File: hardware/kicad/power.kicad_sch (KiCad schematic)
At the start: 46 parts, among them J1 USB_C_Receptacle_USB2.0_16P, J2 BATT (LiFePO4), Q1 AO3401A, U1 MCP73123-22S/MF, U2 TPS63802DLA, U3 TPS61023DRL, U4 TPS22965DSG, U5 USBLC6-2SC6, U6 TPS63900DSK

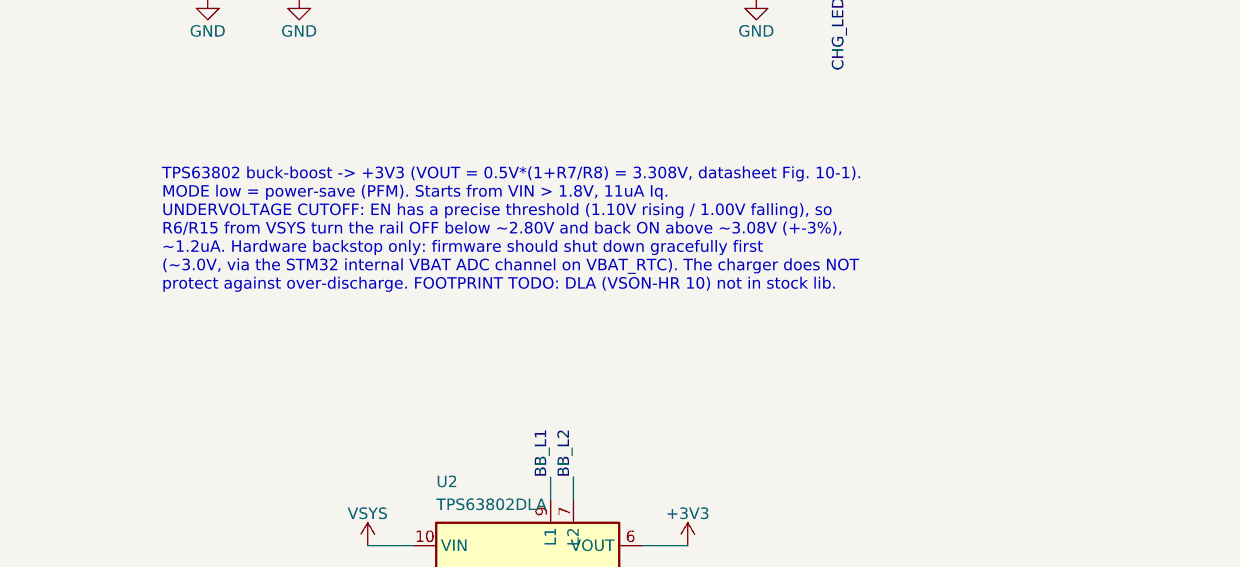
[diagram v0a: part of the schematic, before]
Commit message: Add TPS63802 DLA0010A footprint (project library)
hardware/kicad/epaper.pretty: VSON-HR 10 (2x3 mm HotRod) land pattern
transcribed from the TPS63802 datasheet (SLVSEU9D pp. 35-37), including the
split paste apertures on the pin-8 GND bar (83% coverage). Generated by
hardware/scripts/gen_footprints.py; assigned to U2 via a project
fp-lib-table. ERC 0 violations, power netlist check 34/34.

Co-Authored-By: Claude Opus 5.5 <noreply@anthropic.com>
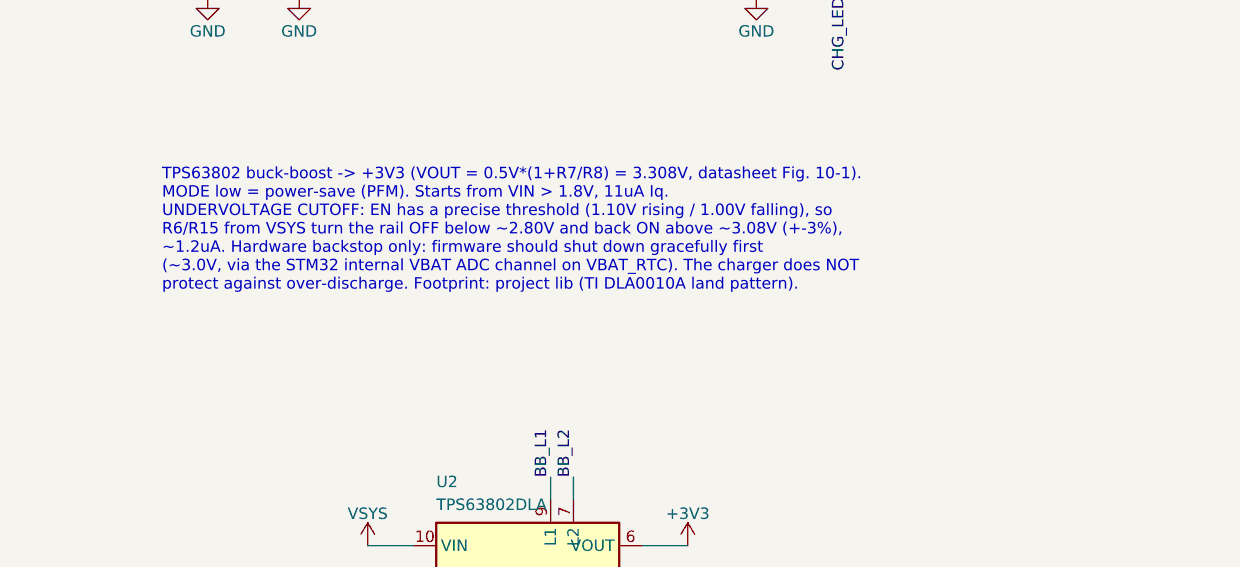
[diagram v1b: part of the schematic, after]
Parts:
- U2: footprint (none) -> epaper:Texas_DLA0010A_VSON-HR-10_2x3mm_P0.5mm
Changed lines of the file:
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@@
 		)
 	)
-	(text "TPS63802 buck-boost -> +3V3 (VOUT = 0.5V*(1+R7/R8) = 3.308V, datasheet Fig. 10-1).\nMODE low = power-save (PFM). Starts from VIN > 1.8V, 11uA Iq.\nUNDERVOLTAGE CUTOFF: EN has a precise threshold (1.10V rising / 1.00V falling), so\nR6/R15 from VSYS turn the rail OFF below ~2.80V and back ON above ~3.08V (+-3%),\n~1.2uA. Hardware backstop only: firmware should shut down gracefully first\n(~3.0V, via the STM32 internal VBAT ADC channel on VBAT_RTC). The charger does NOT\nprotect against over-discharge. FOOTPRINT TODO: DLA (VSON-HR 10) not in stock lib."
+	(text "TPS63802 buck-boost -> +3V3 (VOUT = 0.5V*(1+R7/R8) = 3.308V, datasheet Fig. 10-1).\nMODE low = power-save (PFM). Starts from VIN > 1.8V, 11uA Iq.\nUNDERVOLTAGE CUTOFF: EN has a precise threshold (1.10V rising / 1.00V falling), so\nR6/R15 from VSYS turn the rail OFF below ~2.80V and back ON above ~3.08V (+-3%),\n~1.2uA. Hardware backstop only: firmware should shut down gracefully first\n(~3.0V, via the STM32 internal VBAT ADC channel on VBAT_RTC). The charger does NOT\nprotect against over-discharge. Footprint: project lib (TI DLA0010A land pattern)."
 		(exclude_from_sim no)
 		(at 137.16 129.54 0)
@@
 			)
 		)
-		(property "Footprint" ""
+		(property "Footprint" "epaper:Texas_DLA0010A_VSON-HR-10_2x3mm_P0.5mm"
 			(at 177.8 175.26 0)
 			(hide yes)

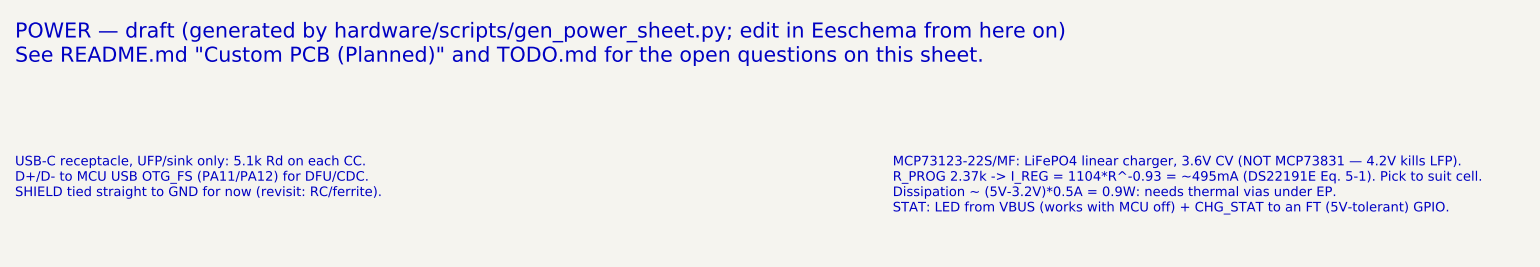
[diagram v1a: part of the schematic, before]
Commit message: Add MCU, Memory and Peripherals sheets; whole-schematic checker
- MCU (A2): STM32F469IIT6 LQFP176. Pin assignment lives in
  sheet_mcu.PINMAP and follows the F469-Disco (FMC SDRAM now 16-bit, QSPI,
  SDIO, SPI1 + HAT control pins, USART3 log UART, I2C1) so the firmware
  config carries over. SD card-detect moved PG2 -> PG10 to keep EXTI2 for
  HRDY. DS11189 power scheme: 13x100nF + 4.7uF, VDDUSB, ferrite-fed
  VDDA/VREF+, 2x2.2uF VCAP; DSI unused per DS11189 2.18 (VDDDSI->VDD,
  VCAPDSI->VDD12DSI, no cap). 8 MHz HSE, 32.768 kHz LSE, BOOT button for
  ROM DFU (BOOT1/PB2 pulled low), TC2050 SWD+SWO, UART header, status LED,
  1k series on the PA9 VBUS sense.
- Memory: IS42S16400J (8 MB), W25Q128JV QSPI, Molex 104031-0811 microSD
  with detect switch and 47k pull-ups, all on 3V3_PERIPH.
- Peripherals: 1x8 header for the external IT8951 HAT (33R series on
  SCK/MOSI/CS), CAP1188 (I2C addr 0x29, 4 electrode pads), PEC11R encoder
  with Bourns' filter, WKUP power button (active high).
- New project symbol CAP1188 and footprint PEC11R-4xxxF-Sxxxx (datasheet
  PCB layout; the Alps EC11E footprint does not fit, its tabs are 11.2 mm
  apart vs 13.2 mm).
- Generator split into common.py + one module per sheet (gen_schematic.py);
  check_schematic.py replaces check_power_netlist.py and adds pin-mux
  (required alternate function per pin), memory-bus end-to-end,
  single-connection-net and pin-vs-footprint-pad checks.

ERC: 0 violations. check_schematic.py: 187 nets, 83 MCU pins, 604 pin/pad
connections OK. All 83 assigned pin numbers also cross-checked by hand
against the DS11189 LQFP176 pin table.

Co-Authored-By: Claude Opus 5.5 <noreply@anthropic.com>
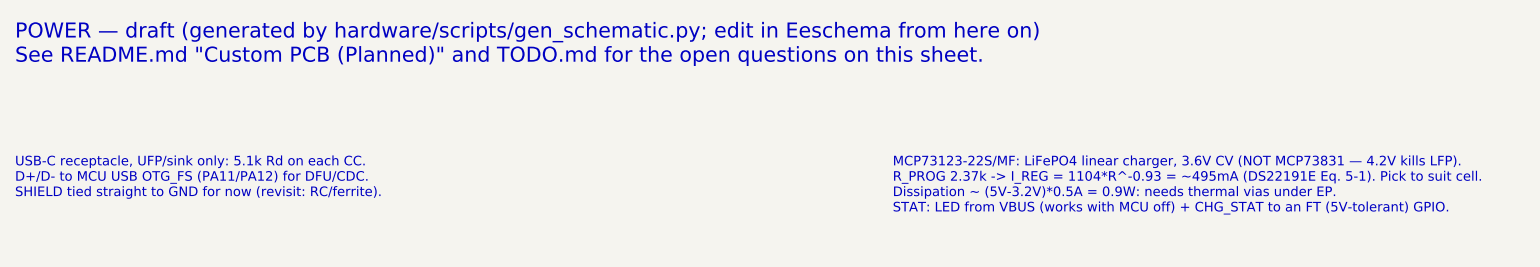
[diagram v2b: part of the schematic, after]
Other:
- note added: "POWER — draft (generated by hardware/scripts/gen_schematic.py; edit in Eeschema from here on) See README.md "Custom PCB (Planned)" and TODO.md for the open questions on this sheet."
- note removed: "POWER — draft (generated by hardware/scripts/gen_power_sheet.py; edit in Eeschema from here on) See README.md "Custom PCB (Planned)" and TODO.md for the open questions on this sheet."

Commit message: Finish v1 schematic: rail test points, docs, deterministic generation
- Power sheet: test points on VBUS/VSYS/+BATT/+3V3/+5V/GND for bring-up;
  R13/R18 0R links (carry all peripheral / MCU current on v1) 0402 -> 0603.
- kicad_gen: UUIDs derived deterministically per sheet (uuid5 of sheet +
  item order), so regenerating produces diffs only where the design changed.
- README: status, pin-assignment table, MCU/memory/peripheral decisions,
  "Checking the Schematic", repo layout. TODO: schematic marked drafted,
  remaining schematic open items (human review, crystals, electrode
  geometry, ESD, HRDY, firmware changes for the custom board), PCB layout
  as the next milestone.

ERC 0 violations; check_schematic.py OK (187 nets, 83 MCU pins, 34
power-sheet nets, all pins present on their footprints).

Co-Authored-By: Claude Opus 5.5 <noreply@anthropic.com>
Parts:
- added TP1: VBUS, TestPoint:TestPoint_Pad_D1.5mm, symbol Connector:TestPoint
- added TP2: VSYS, TestPoint:TestPoint_Pad_D1.5mm, symbol Connector:TestPoint
- added TP3: +BATT, TestPoint:TestPoint_Pad_D1.5mm, symbol Connector:TestPoint
- added TP4: +3V3, TestPoint:TestPoint_Pad_D1.5mm, symbol Connector:TestPoint
- added TP5: +5V, TestPoint:TestPoint_Pad_D1.5mm, symbol Connector:TestPoint
- added TP6: GND, TestPoint:TestPoint_Pad_D1.5mm, symbol Connector:TestPoint
- R13, R18: footprint Resistor_SMD:R_0402_1005Metric -> Resistor_SMD:R_0603_1608Metric
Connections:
- net +3V3: now also TP4.1
- net +5V: now also TP5.1
- net +BATT: now also TP3.1
- net GND: now also TP6.1
- net VBUS: now also TP1.1
- net VSYS: now also TP2.1
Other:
- note added: "Bring-up test points (one per rail)."

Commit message: Switch battery chemistry from LiFePO4 to 1-cell LiPo pouch
Small flat LFP pouches aren't practically buyable in the US; protected LiPo
pouches with JST-PH leads are stocked everywhere.

Power sheet:
- MCP73123 (3.6 V LFP) + discrete AN1149 load sharing (D1/Q1/R5) ->
  TI BQ24073: 4.2 V CV, power path with OUT (VSYS) regulated to 4.4 V so
  the 5.5 V-max TPS63802/TPS61023 stay safe, USB500 input limit, ~500 mA
  charge (ISET 1.78k), ILIM 1.54k fitted (open ILIM disables charging),
  on-board 10k NTC on TS (0-50 C charge window).
- RTC backup: BAT54J -> MCP1700 3.0 V LDO (4.2 V minus a diode drop would
  exceed VBAT's 3.6 V max).
- New VBAT_SENSE 1M/1M divider to PA3 (ADC1_IN3) for the firmware cutoff and
  fuel estimate (VBAT_RTC is now clamped by the LDO).
- UVLO divider on TPS63802 EN 1.8M/1M -> 2.2M/1M (off ~3.20 V, on ~3.52 V).
- MCP73123 project symbol removed; redundant VBAT_RTC PWR_FLAG removed.

README/TODO: chemistry rationale and trade-offs, new power tree, battery
protection layers, updated sheet notes and open items (cell choice, NTC
coupling, fitting the peripheral load switch on v1).

ERC 0 violations; check_schematic.py OK (190 nets, 84 MCU pins, 38 power-
sheet nets); PA3 pin number cross-checked against DS11189.

Co-Authored-By: Claude Opus 5.5 <noreply@anthropic.com>
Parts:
- removed D1: PMEG2010AEH, Diode_SMD:D_SOD-123F, symbol Device:D_Schottky
- removed D3: BAT54J, Diode_SMD:D_SOD-323F, symbol Device:D_Schottky
- removed Q1: AO3401A, Package_TO_SOT_SMD:SOT-23, symbol Transistor_FET:AO3401A
- removed R5: 10k, Resistor_SMD:R_0402_1005Metric, symbol Device:R
- added C15: 10uF, Capacitor_SMD:C_0603_1608Metric, symbol Device:C
- added C16: 1uF, Capacitor_SMD:C_0402_1005Metric, symbol Device:C
- added C17: 100nF, Capacitor_SMD:C_0402_1005Metric, symbol Device:C
- added R19: 1.54k 1%, Resistor_SMD:R_0402_1005Metric, symbol Device:R
- added R20: 100k, Resistor_SMD:R_0402_1005Metric, symbol Device:R
- added R21, R22: 1M 1%, Resistor_SMD:R_0402_1005Metric, symbol Device:R
- added RT1: 10k NTC, Resistor_SMD:R_0402_1005Metric, symbol Device:Thermistor_NTC
- added U7: MCP1700T-3002E/TT, Package_TO_SOT_SMD:SOT-23, symbol Regulator_Linear:MCP1700x-300xxTT
- C1: Voltage (none) -> 10V
- C2: value 4.7uF -> 10uF; Voltage (none) -> 10V
- C3: value 100nF -> 1uF
- J2: value BATT (LiFePO4) -> BATT (1S LiPo)
- R3: value 2.37k 1% -> 1.78k 1%
- R6: value 1.8M 1% -> 2.2M 1%
- U1: value MCP73123-22S/MF -> BQ24073RGT; footprint Package_DFN_QFN:DFN-10-1EP_3x3mm_P0.5mm_EP1.55x2.48mm -> Package_DFN_QFN:VQFN-16-1EP_3x3mm_P0.5mm_EP1.6x1.6mm; symbol epaper:MCP73123 -> Battery_Management:BQ24073RGT; MPN MCP73123-22SI/MF -> BQ24073RGTR
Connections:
- net +BATT: now also U1.2 (BAT), C16.1, R21.1, U7.3 (VI); no longer U1.4 (VBAT)
- net CHG_STAT: now also U1.9 (~{CHG}); no longer U1.7 (STAT)
- net GND: now also U1.15 (TD), U1.17 (VSS), U1.4 (~{CE}), U1.5 (EN2), C15.2, C16.2, C17.2, R19.2, R22.2, RT1.2, U7.1 (GND); no longer U1.11 (EP), U1.9 (VSS)
- net VBAT_RTC: now also U7.2 (VO)
- net VBUS: now also U1.13 (IN), R20.1; no longer U1.1 (VDD), U1.2 (VDD)
- net VSYS: now also U1.10 (OUT), U1.11 (OUT), C15.1
- net CHG_EN1: now reaches U1.6 (EN1)
- net CHG_EN1: now also R20.2
- net PROG renamed ISET
- net ISET: now also U1.16 (ISET); no longer U1.10 (PROG)
- new net ILIM: R19.1, U1.12 (ILIM)
- new net TS: RT1.1, U1.1 (TS)
- new net VBAT_SENSE: C17.1, R21.2, R22.1
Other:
- note added: "BQ24073 1-cell Li-ion/LiPo charger with power path (TI SLUS810N): 4.2V CV, OUT = VSYS regulated to 4.4V with USB present (keeps the 5.5V-max converters safe), battery supplement when the load exceeds the input limit, 6.6V input OVP. ISET 1.78k -> 890/1.78k = ~500mA charge (0.4-0.5C for a 1-1.2Ah cell; retune to cell). EN2=0/EN1=1 -> USB500 input limit (USB-C default power, no CC advertisement rea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"
- note added: "Battery: 1-cell LiPo pouch (3.7V nominal, 4.2V full) WITH a protection board, JST-PH 2.0 lead. J2 pin 1 = + (Adafruit/SparkFun cells: check polarity before plugging in - it is not standardised across vendors). Power path is inside U1, so no discrete load-sharing parts are needed."
- note added: "Cell voltage sense for firmware (fuel estimate + graceful shutdown at ~3.4V): 1M/1M divider -> VBAT_SENSE (4.2V -> 2.1V) to PA3 / ADC1_IN3, 100nF for the ADC sample. ~2uA continuous. (VBAT_RTC can no longer be used: it sits behind the 3.0V LDO.)"
- note added: "RTC backup: cell -> MCP1700 3.0V LDO (1.6uA Iq) -> STM32 VBAT. A full LiPo (4.2V) minus a Schottky drop would still exceed VBAT's 3.6V max. Below ~3.2V the LDO drops out and VBAT tracks the cell (VBAT min 1.65V)."
- note added: "TPS63802 buck-boost -> +3V3 (VOUT = 0.5V*(1+R7/R8) = 3.308V, datasheet Fig. 10-1). MODE low = power-save (PFM). Starts from VIN > 1.8V, 11uA Iq. UNDERVOLTAGE CUTOFF: EN has a precise threshold (1.10V rising / 1.00V falling), so R6/R15 (2.2M/1M) from VSYS turn the rail OFF below ~3.20V and back ON above ~3.52V (+-3%), ~1.1uA. Backstop only: firmware shuts down gracefully first (~3.4V, measured via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"
- note removed: "Battery: JST-PH 2-pin (pin 1 = +). CHECK cell lead polarity — not standardised. Load sharing (Microchip AN1149): with USB present, D1 feeds VSYS from VBUS and Q1 is off, so the charger sees only the cell and terminates correctly. On battery, R5 pulls Q1 gate low -> Q1 on, cell feeds VSYS. R5 = 10k (not 100k) so D1 reverse leakage (tens of uA hot) cannot lift the gate and half-close Q1."
- note removed: "MCP73123-22S/MF: LiFePO4 linear charger, 3.6V CV (NOT MCP73831 — 4.2V kills LFP). R_PROG 2.37k -> I_REG = 1104*R^-0.93 = ~495mA (DS22191E Eq. 5-1). Pick to suit cell. Dissipation ~ (5V-3.2V)*0.5A = 0.9W: needs thermal vias under EP. STAT: LED from VBUS (works with MCU off) + CHG_STAT to an FT (5V-tolerant) GPIO."
- note removed: "RTC backup: cell -> Schottky -> STM32 VBAT. Full LFP 3.65V - ~0.3V drop keeps VBAT under its 3.6V max."
- note removed: "TPS63802 buck-boost -> +3V3 (VOUT = 0.5V*(1+R7/R8) = 3.308V, datasheet Fig. 10-1). MODE low = power-save (PFM). Starts from VIN > 1.8V, 11uA Iq. UNDERVOLTAGE CUTOFF: EN has a precise threshold (1.10V rising / 1.00V falling), so R6/R15 from VSYS turn the rail OFF below ~2.80V and back ON above ~3.08V (+-3%), ~1.2uA. Hardware backstop only: firmware should shut down gracefully first (~3.0V, via the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"

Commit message: Finalize charger for the chosen EEMB cells; battery bay dimensions
From EEMB's LP963450-PCM-LD pack spec and LP603449 cell spec:
- Charge current 500 mA -> ~296 mA (ISET 3.01k, 265-324 mA worst case):
  <= 0.3C of the 1100 mAh cell, EEMB's limit for charging at 0-20 C.
- TMR 72k: fast-charge timer 7.2-12 h (default 4-6 h would expire on the
  1800 mAh cell at ~300 mA).
- Cells allow charging only at 0-45 C; the BQ24073 window is ~0-50 C and TI's
  Rs/Rp network can only widen it (needs an NTC resistance ratio >= 7 across
  the window). So CE -> CHG_DIS (PD6, 100k pull-down keeps charging on with
  the MCU off) and TS -> TS_SENSE (10k/100nF to PC1, ADC1_IN11) for firmware
  supervision of the hot end.
- README: pack specs (PCM 3.0 V over-discharge / 4.28 V overcharge, 1 A
  continuous, 50 mm AWG26 leads), battery bay envelope (52 x 34.5 x 9.9 mm
  max + swelling allowance, lead exit edge), pin table. TODO: firmware
  charge-temperature supervision; arrival checks.

ERC 0 violations; check_schematic.py OK (190 nets, 86 MCU pins, 40 power-
sheet nets); PD6/PC1 pin numbers cross-checked against DS11189.

Co-Authored-By: Claude Opus 5.5 <noreply@anthropic.com>
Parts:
- removed C5, C6: 10uF, Capacitor_SMD:C_0603_1608Metric, symbol Device:C
- removed L1: 0.47uH, Inductor_SMD:L_Murata_DFE201610P, symbol Device:L
- removed L2: 1uH, Inductor_SMD:L_Murata_DFE201610P, symbol Device:L
- removed R14, R17: 100k, Resistor_SMD:R_0402_1005Metric, symbol Device:R
- added C12: 22uF, Capacitor_SMD:C_0805_2012Metric, symbol Device:C
- added C2: 10uF, Capacitor_SMD:C_0603_1608Metric, symbol Device:C
- added C7, C9: 22uF, Capacitor_SMD:C_0603_1608Metric, symbol Device:C
- added R18: 0R, Resistor_SMD:R_0603_1608Metric, symbol Device:R
- added R23: 72k 1%, Resistor_SMD:R_0402_1005Metric, symbol Device:R
- added R24: 100k, Resistor_SMD:R_0402_1005Metric, symbol Device:R
- added R25: 10k, Resistor_SMD:R_0402_1005Metric, symbol Device:R
- added R7: 511k 1%, Resistor_SMD:R_0402_1005Metric, symbol Device:R
- added TP4: +3V3, TestPoint:TestPoint_Pad_D1.5mm, symbol Connector:TestPoint
- C18: renamed from C2; value 10uF -> 100nF; footprint Capacitor_SMD:C_0603_1608Metric -> Capacitor_SMD:C_0402_1005Metric; Voltage 10V -> (none)
- C5: renamed from R7; value 511k 1% -> 10uF; footprint Resistor_SMD:R_0402_1005Metric -> Capacitor_SMD:C_0603_1608Metric; symbol Device:R -> Device:C; Voltage (none) -> 10V
- C6: renamed from C7; value 22uF -> 10uF
- L1: renamed from C9; value 22uF -> 0.47uH; footprint Capacitor_SMD:C_0603_1608Metric -> Inductor_SMD:L_Murata_DFE201610P; symbol Device:C -> Device:L; MPN (none) -> DFE201612E-R47M (TI Table 10-2: 5.5A Isat; verify land patt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
- L2: renamed from C12; value 22uF -> 1uH; footprint Capacitor_SMD:C_0805_2012Metric -> Inductor_SMD:L_Murata_DFE201610P; symbol Device:C -> Device:L; MPN (none) -> DFE201610P-1R0M (verify Isat vs 3.7A valley limit)
- R14: renamed from TP4; value +3V3 -> 100k; footprint TestPoint:TestPoint_Pad_D1.5mm -> Resistor_SMD:R_0402_1005Metric; symbol Connector:TestPoint -> Device:R; now not fitted
- R17: renamed from R18; value 0R -> 100k; footprint Resistor_SMD:R_0603_1608Metric -> Resistor_SMD:R_0402_1005Metric; now not fitted
- R3: value 1.78k 1% -> 3.01k 1%
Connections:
- net +3V3: now also C9.1, R18.1, R7.1, TP4.1; no longer C5.1, L1.1, R14.1, R17.1
- net +5V: now also C12.1; no longer L2.1
- net +BATT: now also C2.1; no longer C18.1
- net 3V3_AON: now also C7.1, R18.2; no longer C6.1, R17.2
- net AON_EN: now also R17.2
- net BB_FB: now also R7.2; no longer C5.2
- net BB_L1: now also L1.1
- net BB_L2: now also L1.2
- net BST_SW: now also L2.2
- net GND: now also C5.2, R14.2, C12.2, C2.2, C7.2, C9.2, R23.2, R24.2; no longer L1.2, L2.2, U1.4 (~{CE})
- net PERIPH_EN: now also R14.1
- net TS: now also R25.1
- net VSYS: now also C5.1, C6.1, L2.1, R17.1
- net TMR: now reaches U1.14 (TMR)
- net TMR: now also R23.1
- new net CHG_DIS: R24.1, U1.4 (~{CE})
- new net TS_SENSE: C18.1, R25.2
- no-connect marks 4 -> 3
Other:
- note added: "BQ24073 1-cell Li-ion/LiPo charger with power path (TI SLUS810N): 4.2V CV, OUT = VSYS regulated to 4.4V with USB present (keeps the 5.5V-max converters safe), battery supplement when the load exceeds the input limit, 6.6V input OVP. ISET 3.01k -> 890/3.01k = ~296mA (265-324mA worst case): <= 0.3C of the 1100mAh cell, which is EEMB's limit for charging at 0-20C (either candidate cell is in spec an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"
- note removed: "BQ24073 1-cell Li-ion/LiPo charger with power path (TI SLUS810N): 4.2V CV, OUT = VSYS regulated to 4.4V with USB present (keeps the 5.5V-max converters safe), battery supplement when the load exceeds the input limit, 6.6V input OVP. ISET 1.78k -> 890/1.78k = ~500mA charge (0.4-0.5C for a 1-1.2Ah cell; retune to cell). EN2=0/EN1=1 -> USB500 input limit (USB-C default power, no CC advertisement rea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"
- moved on the sheet: C18, C6
